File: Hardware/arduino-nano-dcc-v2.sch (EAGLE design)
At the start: 45 parts, among them IC1 7805TV, IC3 MEGA328-P, Q2 TIP41C, X1 22-23-2031

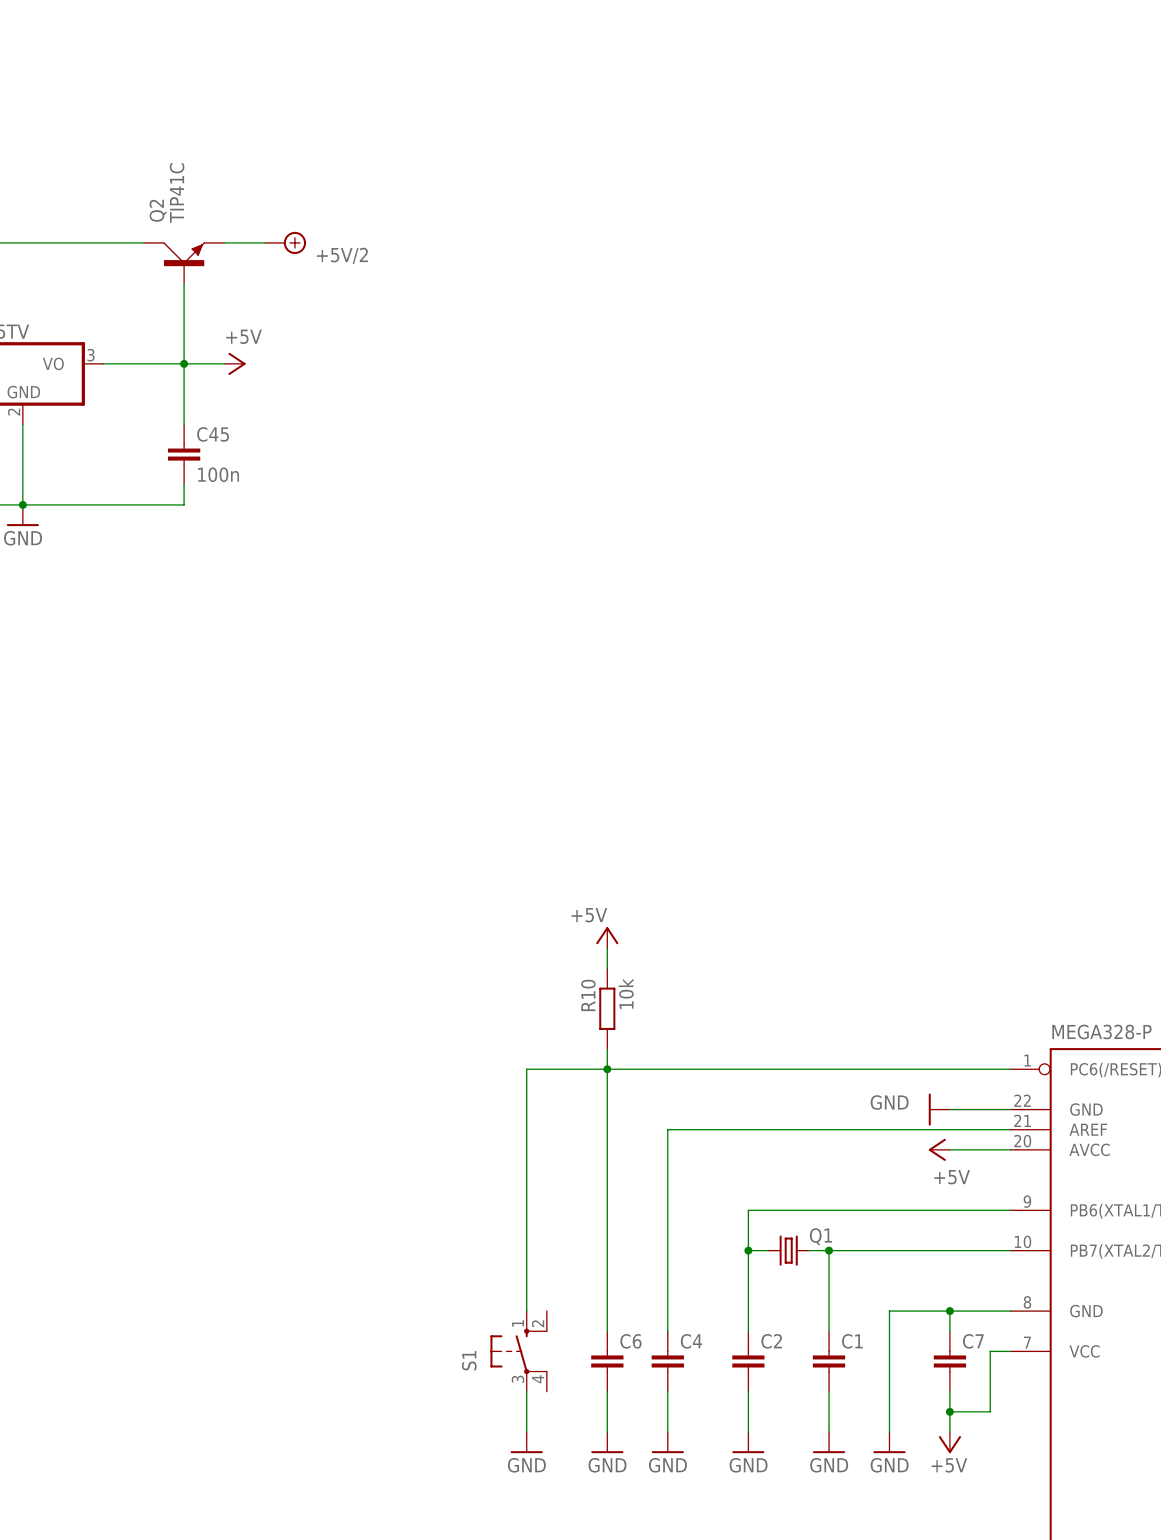
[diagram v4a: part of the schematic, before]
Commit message: Added values to components and added partlist.
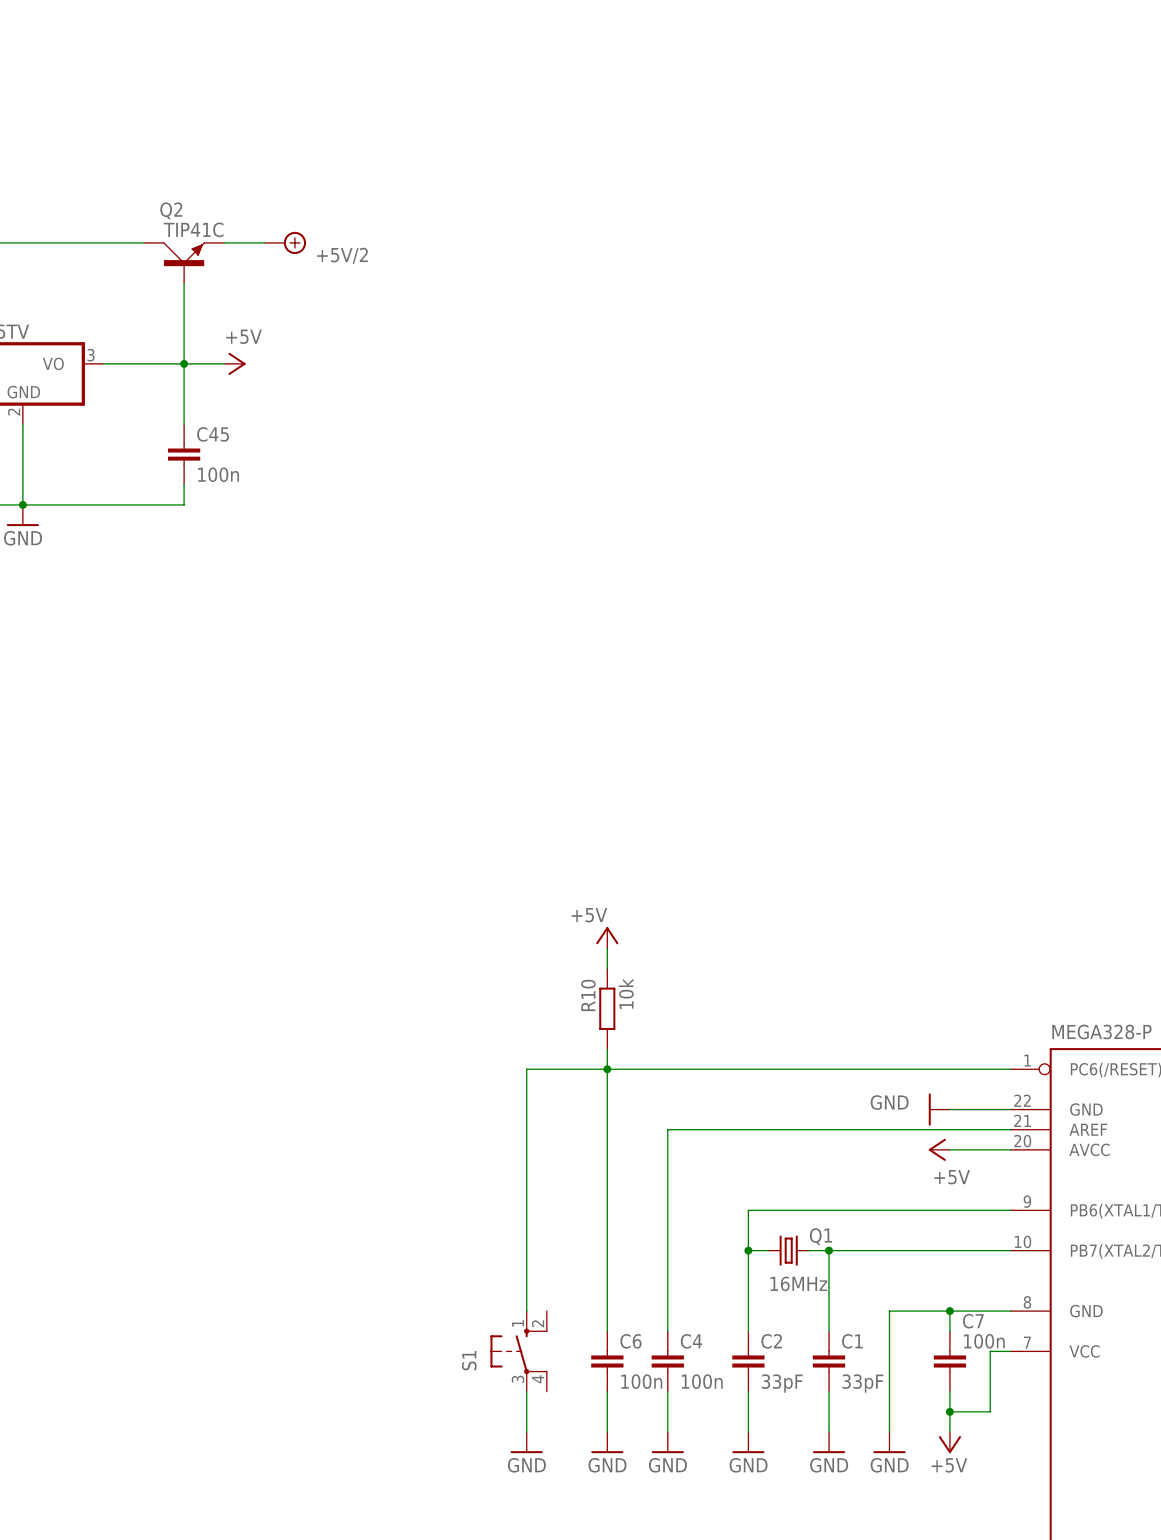
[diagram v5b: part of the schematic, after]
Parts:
- C1, C2: value (none) -> 33pF
- C4, C6, C7: value (none) -> 100n
- Q1: value (none) -> 16MHz
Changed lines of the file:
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@@
 <part name="IC3" library="atmel" library_urn="urn:adsk.eagle:library:105" deviceset="MEGA8-P" device="" package3d_urn="urn:adsk.eagle:package:4320/1" value="MEGA328-P"/>
 <part name="FRAME1" library="frames" library_urn="urn:adsk.eagle:library:229" deviceset="DINA3_L" device=""/>
-<part name="Q1" library="crystal" library_urn="urn:adsk.eagle:library:204" deviceset="CRYSTAL" device="HC49U-V" package3d_urn="urn:adsk.eagle:package:12075/1"/>
-<part name="C1" library="rcl" library_urn="urn:adsk.eagle:library:334" deviceset="C-EU" device="025-024X044" package3d_urn="urn:adsk.eagle:package:23630/1"/>
-<part name="C2" library="rcl" library_urn="urn:adsk.eagle:library:334" deviceset="C-EU" device="025-024X044" package3d_urn="urn:adsk.eagle:package:23630/1"/>
-<part name="C4" library="rcl" library_urn="urn:adsk.eagle:library:334" deviceset="C-EU" device="050-024X044" package3d_urn="urn:adsk.eagle:package:23643/1"/>
+<part name="Q1" library="crystal" library_urn="urn:adsk.eagle:library:204" deviceset="CRYSTAL" device="HC49U-V" package3d_urn="urn:adsk.eagle:package:12075/1" value="16MHz"/>
+<part name="C1" library="rcl" library_urn="urn:adsk.eagle:library:334" deviceset="C-EU" device="025-024X044" package3d_urn="urn:adsk.eagle:package:23630/1" value="33pF"/>
+<part name="C2" library="rcl" library_urn="urn:adsk.eagle:library:334" deviceset="C-EU" device="025-024X044" package3d_urn="urn:adsk.eagle:package:23630/1" value="33pF"/>
+<part name="C4" library="rcl" library_urn="urn:adsk.eagle:library:334" deviceset="C-EU" device="050-024X044" package3d_urn="urn:adsk.eagle:package:23643/1" value="100n"/>
 <part name="GND5" library="supply1" deviceset="GND" device=""/>
 <part name="P+3" library="supply1" library_urn="urn:adsk.eagle:library:371" deviceset="+5V" device=""/>
 <part name="P+4" library="supply1" library_urn="urn:adsk.eagle:library:371" deviceset="+5V" device=""/>
 <part name="R10" library="rcl" deviceset="R-EU_" device="0204/7" value="10k"/>
-<part name="C6" library="rcl" library_urn="urn:adsk.eagle:library:334" deviceset="C-EU" device="050-024X044" package3d_urn="urn:adsk.eagle:package:23643/1"/>
-<part name="C7" library="rcl" library_urn="urn:adsk.eagle:library:334" deviceset="C-EU" device="050-024X044" package3d_urn="urn:adsk.eagle:package:23643/1"/>
+<part name="C6" library="rcl" library_urn="urn:adsk.eagle:library:334" deviceset="C-EU" device="050-024X044" package3d_urn="urn:adsk.eagle:package:23643/1" value="100n"/>
+<part name="C7" library="rcl" library_urn="urn:adsk.eagle:library:334" deviceset="C-EU" device="050-024X044" package3d_urn="urn:adsk.eagle:package:23643/1" value="100n"/>
 <part name="P+5" library="supply1" library_urn="urn:adsk.eagle:library:371" deviceset="+5V" device=""/>
 <part name="GND6" library="supply1" deviceset="GND" device=""/>
@@
 <instance part="Q1" gate="G$1" x="157.48" y="60.96" smashed="yes">
 <attribute name="NAME" x="160.02" y="61.976" size="1.778" layer="95"/>
-<attribute name="VALUE" x="160.02" y="58.42" size="1.778" layer="96"/>
+<attribute name="VALUE" x="154.94" y="55.88" size="1.778" layer="96"/>
 </instance>
 <instance part="C1" gate="G$1" x="162.56" y="48.26" smashed="yes">
@@
 </instance>
 <instance part="C7" gate="G$1" x="177.8" y="48.26" smashed="yes">
-<attribute name="NAME" x="179.324" y="48.641" size="1.778" layer="95"/>
-<attribute name="VALUE" x="179.324" y="43.561" size="1.778" layer="96"/>
+<attribute name="NAME" x="179.324" y="51.181" size="1.778" layer="95"/>
+<attribute name="VALUE" x="179.324" y="48.641" size="1.778" layer="96"/>
 </instance>
 <instance part="P+5" gate="1" x="134.62" y="101.6" smashed="yes">
@@
 </instance>
 <instance part="Q2" gate="1" x="81.28" y="185.42" smashed="yes" rot="R90">
-<attribute name="NAME" x="78.74" y="190.5" size="1.778" layer="95" rot="R90"/>
-<attribute name="VALUE" x="81.28" y="190.5" size="1.778" layer="96" rot="R90"/>
+<attribute name="NAME" x="81.28" y="193.04" size="1.778" layer="95" rot="R180"/>
+<attribute name="VALUE" x="86.36" y="190.5" size="1.778" layer="96" rot="R180"/>
 </instance>
 <instance part="SUPPLY7" gate="G$1" x="93.98" y="187.96" smashed="yes" rot="MR90">
